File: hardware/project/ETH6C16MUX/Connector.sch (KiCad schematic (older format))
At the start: 3 parts, among them J801 Conn_01x06, J802 Conn_02x09_Odd_Even, J803 C64AC

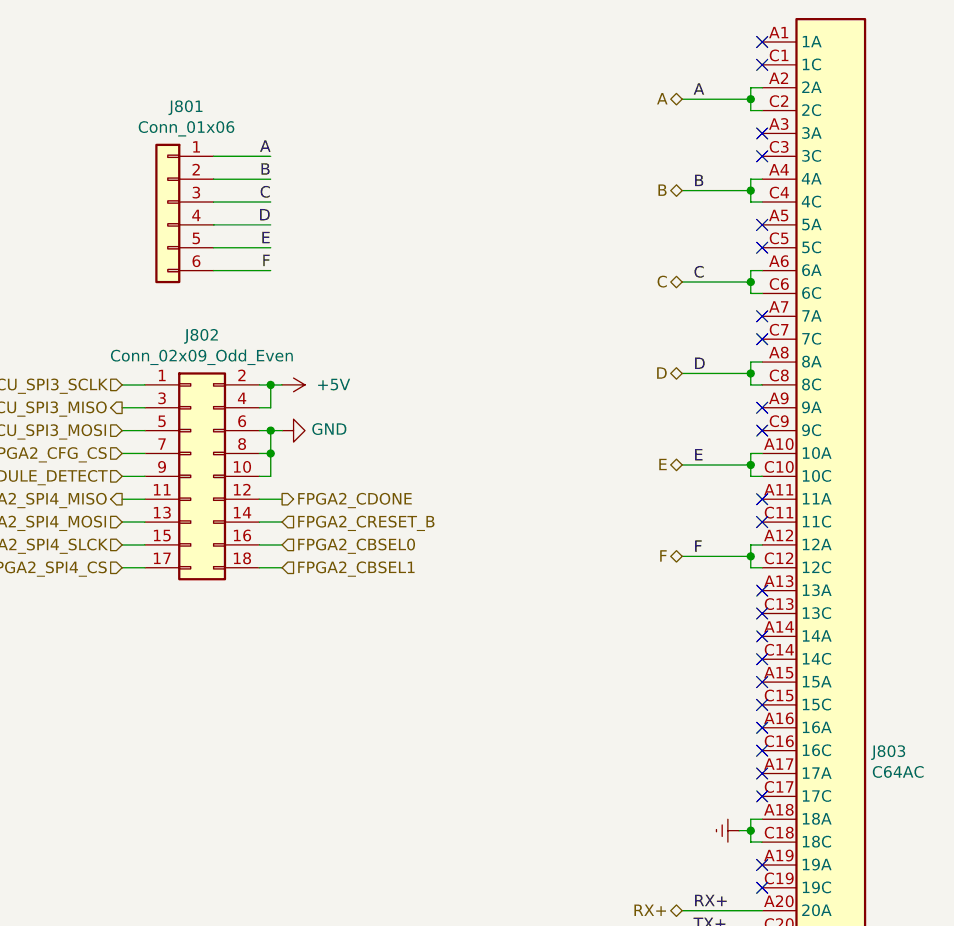
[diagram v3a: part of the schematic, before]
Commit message: PCB layout, deleted USB.
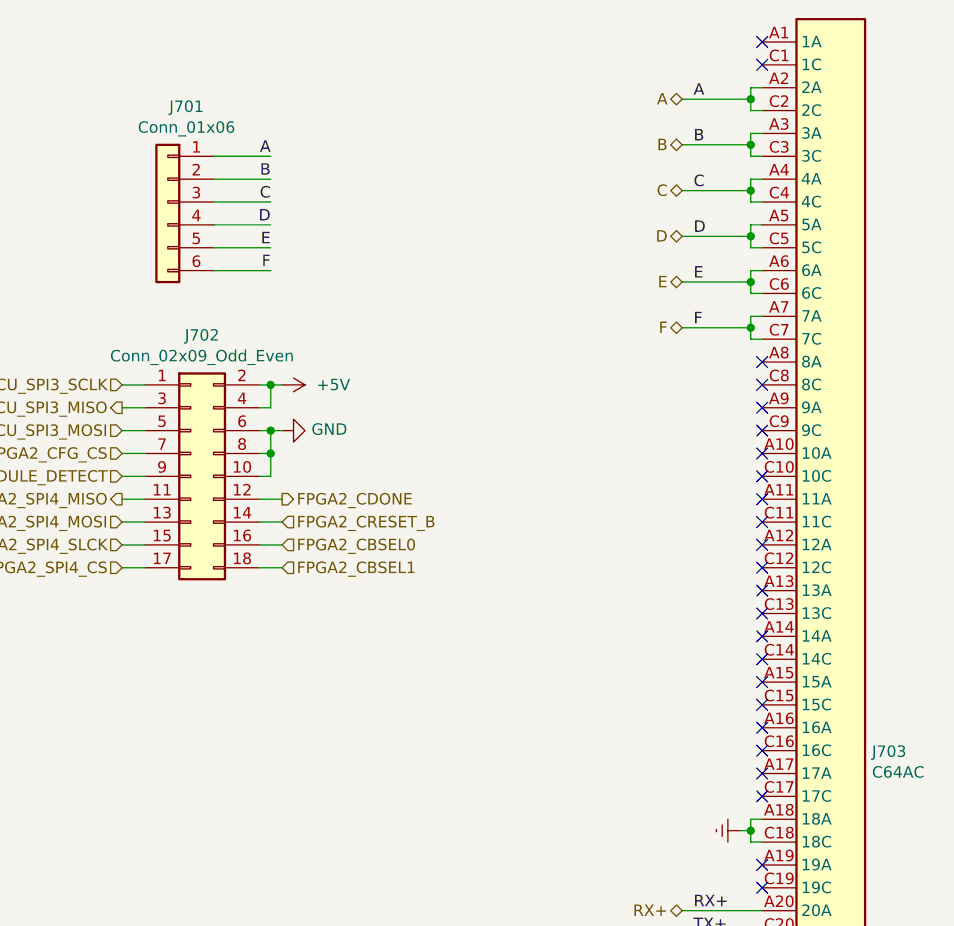
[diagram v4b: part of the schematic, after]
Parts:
- renumbered J801 to J701, J802 to J702, J803 to J703
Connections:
- net B: now also J703.A3 (3A), J703.C3 (3C); no longer J703.A4 (4A), J703.C4 (4C)
- net C: now also J703.A4 (4A), J703.C4 (4C); no longer J703.A6 (6A), J703.C6 (6C)
- net D: now also J703.A5 (5A), J703.C5 (5C); no longer J703.A8 (8A), J703.C8 (8C)
- net E: now also J703.A6 (6A), J703.C6 (6C); no longer J703.A10 (10A), J703.C10 (10C)
- net F: now also J703.A7 (7A), J703.C7 (7C); no longer J703.A12 (12A), J703.C12 (12C)
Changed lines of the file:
@@
 $Descr A4 11693 8268
 encoding utf-8
-Sheet 8 8
+Sheet 7 7
 Title ""
 Date ""
@@
 $EndDescr
 $Comp
-L Connector:C64AC J803
+L Connector:C64AC J703
 U 1 1 5DB3A84B
 P 5950 4000
-F 0 "J803" H 6130 4096 50  0000 L CNN
+F 0 "J703" H 6130 4096 50  0000 L CNN
 F 1 "C64AC" H 6130 4005 50  0000 L CNN
 F 2 "ETH6C16MXU:Socket_DIN41612-CaseC1-AC-Male-64Pin-2rows" H 5950 4050 50  0001 C CNN
@@
 	5600 6200 5600 6100
 $Comp
-L power:+24V #PWR0808
+L power:+24V #PWR0706
 U 1 1 5D7D1F7C
 P 5550 7100
-F 0 "#PWR0808" H 5550 6950 50  0001 C CNN
+F 0 "#PWR0706" H 5550 6950 50  0001 C CNN
 F 1 "+24V" V 5565 7228 50  0000 L CNN
 F 2 "" H 5550 7100 50  0001 C CNN
@@
 Connection ~ 5600 7100
 $Comp
-L power:GND #PWR0807
+L power:GND #PWR0705
 U 1 1 5D7D46BE
 P 5550 6300
-F 0 "#PWR0807" H 5550 6050 50  0001 C CNN
+F 0 "#PWR0705" H 5550 6050 50  0001 C CNN
 F 1 "GND" V 5555 6172 50  0000 R CNN
 F 2 "" H 5550 6300 50  0001 C CNN
@@
 RX-
 $Comp
-L power:Earth #PWR0806
+L power:Earth #PWR0704
 U 1 1 5D7F1666
 P 5550 5050
-F 0 "#PWR0806" H 5550 4800 50  0001 C CNN
+F 0 "#PWR0704" H 5550 4800 50  0001 C CNN
 F 1 "Earth" H 5550 4900 50  0001 C CNN
 F 2 "" H 5550 5050 50  0001 C CNN
@@
 	5600 5050 5600 5000
 $Comp
-L power:Earth #PWR0805
+L power:Earth #PWR0703
 U 1 1 5D7F6C0C
 P 5550 4250
-F 0 "#PWR0805" H 5550 4000 50  0001 C CNN
+F 0 "#PWR0703" H 5550 4000 50  0001 C CNN
 F 1 "Earth" H 5550 4100 50  0001 C CNN
 F 2 "" H 5550 4250 50  0001 C CNN
@@
 	5600 1100 5650 1100
 Wire Wire Line
+	5650 1200 5600 1200
+Wire Wire Line
+	5600 1200 5600 1250
+Wire Wire Line
+	5600 1300 5650 1300
+Wire Wire Line
 	5650 1400 5600 1400
 Wire Wire Line
@@
 	5600 1500 5650 1500
 Wire Wire Line
+	5650 1600 5600 1600
+Wire Wire Line
+	5600 1600 5600 1650
+Wire Wire Line
+	5600 1700 5650 1700
+Wire Wire Line
 	5650 1800 5600 1800
 Wire Wire Line
@@
 	5600 1900 5650 1900
 Wire Wire Line
-	5650 2200 5600 2200
-Wire Wire Line
-	5600 2200 5600 2250
-Wire Wire Line
-	5600 2300 5650 2300
-Wire Wire Line
-	5650 2600 5600 2600
-Wire Wire Line
-	5600 2600 5600 2650
-Wire Wire Line
-	5600 2700 5650 2700
-Wire Wire Line
-	5650 3000 5600 3000
-Wire Wire Line
-	5600 3000 5600 3050
-Wire Wire Line
-	5600 3100 5650 3100
+	5650 2000 5600 2000
+Wire Wire Line
+	5600 2000 5600 2050
+Wire Wire Line
+	5600 2100 5650 2100
 NoConn ~ 5650 4100
 NoConn ~ 5650 4000
@@
 NoConn ~ 5650 2500
 NoConn ~ 5650 2400
-NoConn ~ 5650 2100
-NoConn ~ 5650 2000
-NoConn ~ 5650 1700
-NoConn ~ 5650 1600
-NoConn ~ 5650 1300
-NoConn ~ 5650 1200
 Connection ~ 5600 1050
 Wire Wire Line
 	5600 1050 5600 1100
+Connection ~ 5600 1250
+Wire Wire Line
+	5600 1250 5600 1300
 Connection ~ 5600 1450
 Wire Wire Line
 	5600 1450 5600 1500
+Connection ~ 5600 1650
+Wire Wire Line
+	5600 1650 5600 1700
 Connection ~ 5600 1850
 Wire Wire Line
 	5600 1850 5600 1900
-Connection ~ 5600 2250
-Wire Wire Line
-	5600 2250 5600 2300
-Connection ~ 5600 2650
-Wire Wire Line
-	5600 2650 5600 2700
-Connection ~ 5600 3050
-Wire Wire Line
-	5600 3050 5600 3100
+Connection ~ 5600 2050
+Wire Wire Line
+	5600 2050 5600 2100
 Text HLabel 5300 1050 0    50   BiDi ~ 0
 A
+Text HLabel 5300 1250 0    50   BiDi ~ 0
+B
 Text HLabel 5300 1450 0    50   BiDi ~ 0
-B
+C
+Text HLabel 5300 1650 0    50   BiDi ~ 0
+D
 Text HLabel 5300 1850 0    50   BiDi ~ 0
-C
-Text HLabel 5300 2250 0    50   BiDi ~ 0
-D
-Text HLabel 5300 2650 0    50   BiDi ~ 0
 E
-Text HLabel 5300 3050 0    50   BiDi ~ 0
+Text HLabel 5300 2050 0    50   BiDi ~ 0
 F
 Wire Wire Line
@@
 TX-
 Wire Wire Line
-	5300 3050 5600 3050
-Wire Wire Line
-	5300 2650 5600 2650
-Wire Wire Line
-	5300 2250 5600 2250
+	5300 2050 5600 2050
 Wire Wire Line
 	5300 1850 5600 1850
 Wire Wire Line
+	5300 1650 5600 1650
+Wire Wire Line
 	5300 1450 5600 1450
+Wire Wire Line
+	5300 1250 5600 1250
 Wire Wire Line
 	5300 1050 5600 1050
 Text Label 5350 1050 0    50   ~ 0
 A
+Text Label 5350 1250 0    50   ~ 0
+B
 Text Label 5350 1450 0    50   ~ 0
-B
+C
+Text Label 5350 1650 0    50   ~ 0
+D
 Text Label 5350 1850 0    50   ~ 0
-C
-Text Label 5350 2250 0    50   ~ 0
-D
-Text Label 5350 2650 0    50   ~ 0
 E
-Text Label 5350 3050 0    50   ~ 0
+Text Label 5350 2050 0    50   ~ 0
 F
 Wire Wire Line
@@
 MODULE_DETECT
 $Comp
-L power:GND #PWR0804
+L power:GND #PWR0702
 U 1 1 5D777B58
 P 3550 2500
-AR Path="/5DB25E5A/5D777B58" Ref="#PWR0804"  Part="1"
+AR Path="/5DB25E5A/5D777B58" Ref="#PWR0702"  Part="1"
 AR Path="/5D7599BA/5D777B58" Ref="#PWR?"  Part="1"
-F 0 "#PWR0804" H 3550 2250 50  0001 C CNN
+F 0 "#PWR0702" H 3550 2250 50  0001 C CNN
 F 1 "GND" V 3555 2372 50  0000 R CNN
 F 2 "" H 3550 2500 50  0001 C CNN
@@
 $EndComp
 $Comp
-L power:+5V #PWR0803
+L power:+5V #PWR0701
 U 1 1 5D777B5E
 P 3550 2300
-AR Path="/5DB25E5A/5D777B5E" Ref="#PWR0803"  Part="1"
+AR Path="/5DB25E5A/5D777B5E" Ref="#PWR0701"  Part="1"
 AR Path="/5D7599BA/5D777B5E" Ref="#PWR?"  Part="1"
-F 0 "#PWR0803" H 3550 2150 50  0001 C CNN
+F 0 "#PWR0701" H 3550 2150 50  0001 C CNN
 F 1 "+5V" V 3550 2450 50  0000 L CNN
 F 2 "" H 3550 2300 50  0001 C CNN
@@
 P 3050 1500
 AR Path="/5D7599BA/5D777B7C" Ref="J?"  Part="1"
-AR Path="/5DB25E5A/5D777B7C" Ref="J801"  Part="1"
-F 0 "J801" H 2968 1917 50  0000 C CNN
+AR Path="/5DB25E5A/5D777B7C" Ref="J701"  Part="1"
+F 0 "J701" H 2968 1917 50  0000 C CNN
 F 1 "Conn_01x06" H 2968 1826 50  0000 C CNN
 F 2 "Connector_PinSocket_2.54mm:PinSocket_1x06_P2.54mm_Vertical" H 3050 1500 50  0001 C CNN
@@
 	3250 1800 3500 1800
 $Comp
-L Connector_Generic:Conn_02x09_Odd_Even J802
+L Connector_Generic:Conn_02x09_Odd_Even J702
 U 1 1 5D8AE50E
 P 3150 2700
-F 0 "J802" H 3200 3317 50  0000 C CNN
+F 0 "J702" H 3200 3317 50  0000 C CNN
 F 1 "Conn_02x09_Odd_Even" H 3200 3226 50  0000 C CNN
 F 2 "Connector_PinSocket_2.54mm:PinSocket_2x09_P2.54mm_Vertical" H 3150 2700 50  0001 C CNN
@@
 	3500 2700 3450 2700
 Connection ~ 3500 2600
+NoConn ~ 5650 2200
+NoConn ~ 5650 2300
+NoConn ~ 5650 3000
+NoConn ~ 5650 3100
+NoConn ~ 5650 2600
+NoConn ~ 5650 2700
 $EndSCHEMATC
